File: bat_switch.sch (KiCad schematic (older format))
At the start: 7 parts

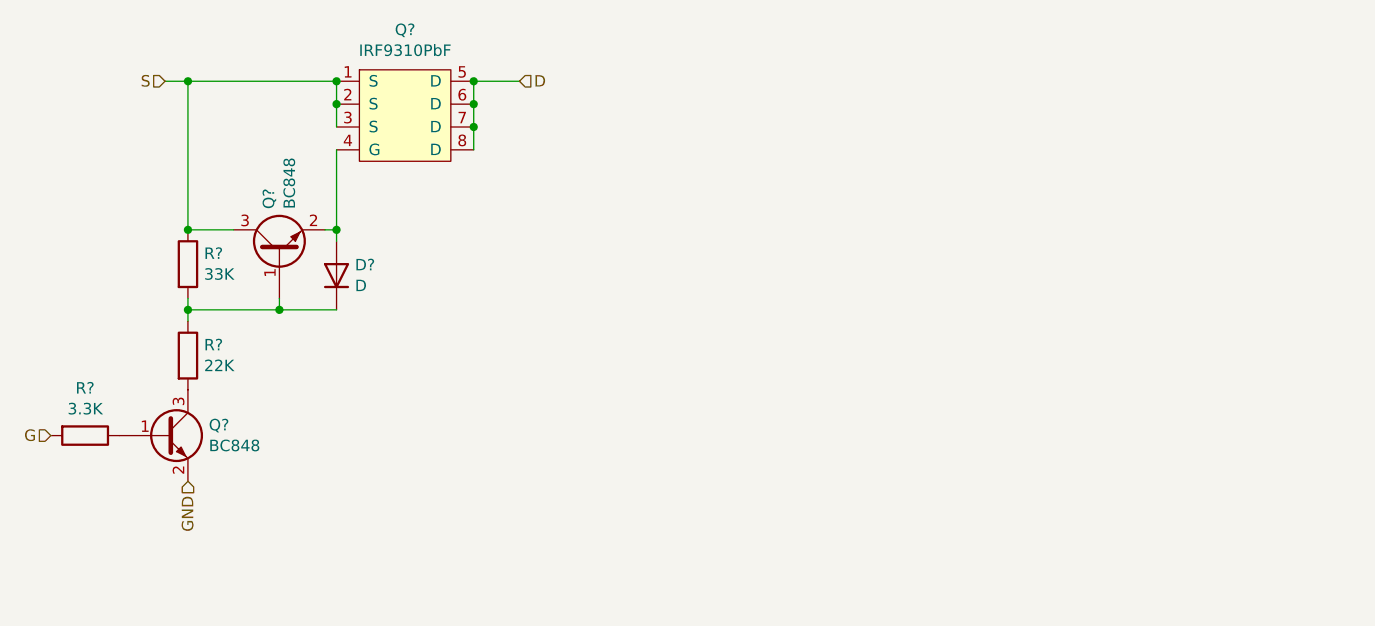
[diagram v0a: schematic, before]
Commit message: Fixes missing footprints, adds initial pcb
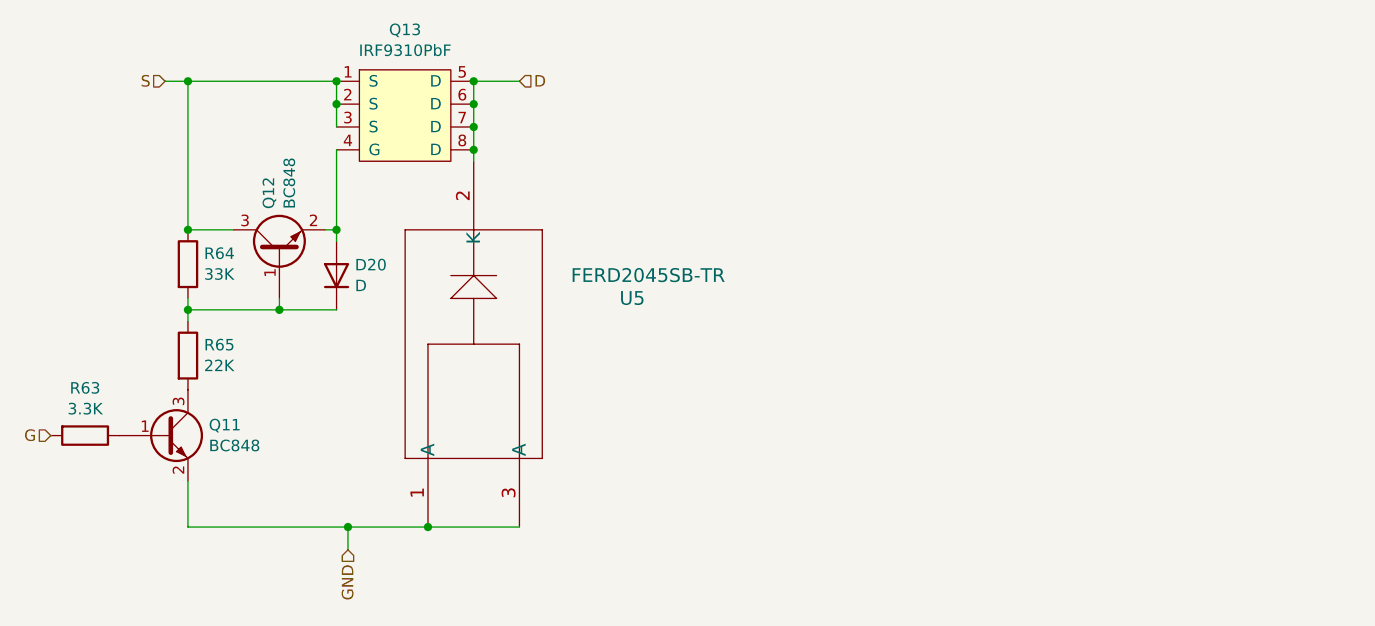
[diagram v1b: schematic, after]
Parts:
- added U5: FERD2045SB-TR, Package_TO_SOT_SMD:TO-263-2_TabPin1, symbol 2021-02-09_22-26-07:FERD2045SB-TR
- D20: renamed from D?; footprint (none) -> Diode_SMD:D_SMA
- gave numbers to parts that had none: 6
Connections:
- net D: now also U5.2 (K)
- net GND: now also U5.1 (A), U5.3 (A)
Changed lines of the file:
@@
 $Descr A4 11693 8268
 encoding utf-8
-Sheet 8 8
+Sheet 7 8
 Title ""
 Date ""
@@
 $EndDescr
 $Comp
-L Transistor_FET:IRF9310PbF Q?
+L Transistor_FET:IRF9310PbF Q13
 U 1 1 6023360E
 P 6050 2700
-F 0 "Q?" H 6050 3075 50  0000 C CNN
+F 0 "Q13" H 6050 3075 50  0000 C CNN
 F 1 "IRF9310PbF" H 6050 2984 50  0000 C CNN
 F 2 "Package_SO:SO-8_3.9x4.9mm_P1.27mm" H 6050 2700 50  0001 C CNN
@@
 $EndComp
 $Comp
-L Transistor_BJT:BC848 Q?
+L Transistor_BJT:BC848 Q11
 U 1 1 60234053
 P 5000 4100
-F 0 "Q?" H 5191 4146 50  0000 L CNN
+F 0 "Q11" H 5191 4146 50  0000 L CNN
 F 1 "BC848" H 5191 4055 50  0000 L CNN
 F 2 "Package_TO_SOT_SMD:SOT-23" H 5200 4025 50  0001 L CIN
@@
 $EndComp
 $Comp
-L Transistor_BJT:BC848 Q?
+L Transistor_BJT:BC848 Q12
 U 1 1 60234344
 P 5500 3300
-F 0 "Q?" H 5691 3346 50  0000 L CNN
+F 0 "Q12" H 5691 3346 50  0000 L CNN
 F 1 "BC848" H 5691 3255 50  0000 L CNN
 F 2 "Package_TO_SOT_SMD:SOT-23" H 5700 3225 50  0001 L CIN
@@
 $EndComp
 $Comp
-L Device:R R?
+L Device:R R63
 U 1 1 602349BB
 P 4650 4100
-F 0 "R?" V 4443 4100 50  0000 C CNN
+F 0 "R63" V 4443 4100 50  0000 C CNN
 F 1 "3.3K" V 4534 4100 50  0000 C CNN
 F 2 "Resistor_SMD:R_0805_2012Metric_Pad1.20x1.40mm_HandSolder" V 4580 4100 50  0001 C CNN
@@
 $EndComp
 $Comp
-L Device:R R?
+L Device:R R65
 U 1 1 60234C8A
 P 5100 3750
-F 0 "R?" H 5170 3796 50  0000 L CNN
+F 0 "R65" H 5170 3796 50  0000 L CNN
 F 1 "22K" H 5170 3705 50  0000 L CNN
 F 2 "Resistor_SMD:R_0805_2012Metric_Pad1.20x1.40mm_HandSolder" V 5030 3750 50  0001 C CNN
@@
 Text HLabel 4500 4100 0    50   Input ~ 0
 G
-Text HLabel 5100 4300 3    50   Input ~ 0
+Text HLabel 5800 4600 3    50   Input ~ 0
 GND
 $Comp
-L Device:R R?
+L Device:R R64
 U 1 1 6023A454
 P 5100 3350
-F 0 "R?" H 5170 3396 50  0000 L CNN
+F 0 "R64" H 5170 3396 50  0000 L CNN
 F 1 "33K" H 5170 3305 50  0000 L CNN
 F 2 "Resistor_SMD:R_0805_2012Metric_Pad1.20x1.40mm_HandSolder" V 5030 3350 50  0001 C CNN
@@
 	5100 3550 5100 3600
 $Comp
-L Device:D D?
+L Device:D D20
 U 1 1 6023F6A8
 P 5750 3400
-F 0 "D?" V 5796 3320 50  0000 R CNN
+F 0 "D20" V 5796 3320 50  0000 R CNN
 F 1 "D" V 5705 3320 50  0000 R CNN
-F 2 "" H 5750 3400 50  0001 C CNN
+F 2 "Diode_SMD:D_SMA" H 5750 3400 50  0001 C CNN
 F 3 "~" H 5750 3400 50  0001 C CNN
 	1    5750 3400
@@
 	6350 2550 6550 2550
 Connection ~ 6350 2550
+$Comp
+L 2021-02-09_22-26-07:FERD2045SB-TR U5
+U 1 1 6024EE1E
+P 6250 4500
+F 0 "U5" V 7250 3650 60  0000 L CNN
+F 1 "FERD2045SB-TR" V 7350 3300 60  0000 L CNN
+F 2 "Package_TO_SOT_SMD:TO-263-2_TabPin1" H 7050 4740 60  0001 C CNN
+F 3 "https://ar.mouser.com/datasheet/2/389/ferd2045s-1849465.pdf" V 7156 4728 60  0001 L CNN
+	1    6250 4500
+	0    -1   -1   0
+$EndComp
+Wire Wire Line
+	6350 2900 6350 2850
+Connection ~ 6350 2850
+Wire Wire Line
+	6550 4500 6150 4500
+Wire Wire Line
+	5100 4500 5100 4300
+Connection ~ 6150 4500
+Wire Wire Line
+	6150 4500 5800 4500
+Wire Wire Line
+	5800 4500 5800 4600
+Connection ~ 5800 4500
+Wire Wire Line
+	5800 4500 5100 4500
 $EndSCHEMATC

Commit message: Added mouser reference.com to charger imput molex pin
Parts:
- Q13: symbol Transistor_FET:IRF9310PbF -> bms_hardware-rescue:IRF9310PbF-Transistor_FET
- U5: symbol 2021-02-09_22-26-07:FERD2045SB-TR -> bms_hardware-rescue:FERD2045SB-TR-2021-02-09_22-26-07
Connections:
- net D: now also U5.3 (K); no longer U5.2 (K)
- net GND: now also U5.2 (A); no longer U5.3 (A)
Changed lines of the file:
@@
 $EndDescr
 $Comp
-L Transistor_FET:IRF9310PbF Q13
+L bms_hardware-rescue:IRF9310PbF-Transistor_FET Q13
 U 1 1 6023360E
 P 6050 2700
@@
 Connection ~ 6350 2550
 $Comp
-L 2021-02-09_22-26-07:FERD2045SB-TR U5
+L bms_hardware-rescue:FERD2045SB-TR-2021-02-09_22-26-07 U5
 U 1 1 6024EE1E
 P 6250 4500

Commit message: add minor changes to schs
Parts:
- U5: footprint Package_TO_SOT_SMD:TO-263-2_TabPin1 -> Package_TO_SOT_SMD:TO-263-3_TabPin2
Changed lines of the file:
@@
 F 0 "U5" V 7250 3650 60  0000 L CNN
 F 1 "FERD2045SB-TR" V 7350 3300 60  0000 L CNN
-F 2 "Package_TO_SOT_SMD:TO-263-2_TabPin1" H 7050 4740 60  0001 C CNN
+F 2 "Package_TO_SOT_SMD:TO-263-3_TabPin2" H 7050 4740 60  0001 C CNN
 F 3 "https://ar.mouser.com/datasheet/2/389/ferd2045s-1849465.pdf" V 7156 4728 60  0001 L CNN
 	1    6250 4500

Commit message: Adds final pcb
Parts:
- removed Q13: IRF9310PbF, Package_SO:SO-8_3.9x4.9mm_P1.27mm, symbol bms_hardware-rescue:IRF9310PbF-Transistor_FET
- removed U5: FERD2045SB-TR, Package_TO_SOT_SMD:TO-263-3_TabPin2, symbol bms_hardware-rescue:FERD2045SB-TR-2021-02-09_22-26-07
- added Q13: IRF9310PbF, Package_SO:SO-8_3.9x4.9mm_P1.27mm, symbol Transistor_FET:IRF9310PbF
- added U5: FERD2045SB-TR, Package_TO_SOT_SMD:TO-252-2, symbol 2021-02-09_22-26-07:FERD2045SB-TR
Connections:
- net D: now also Q13.5 (D), Q13.6 (D), Q13.7 (D), Q13.8 (D), U5.2 (K)
- net GND: now also U5.1 (A), U5.3 (A)
- net S: now also Q13.1 (S), Q13.2 (S), Q13.3 (S)
- net at D20.2 (A), Q12.2 (E): now also Q13.4 (G)
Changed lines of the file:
@@
 $Descr A4 11693 8268
 encoding utf-8
-Sheet 7 8
+Sheet 7 9
 Title ""
 Date ""
@@
 Comment4 ""
 $EndDescr
-$Comp
-L bms_hardware-rescue:IRF9310PbF-Transistor_FET Q13
-U 1 1 6023360E
-P 6050 2700
-F 0 "Q13" H 6050 3075 50  0000 C CNN
-F 1 "IRF9310PbF" H 6050 2984 50  0000 C CNN
-F 2 "Package_SO:SO-8_3.9x4.9mm_P1.27mm" H 6050 2700 50  0001 C CNN
-F 3 "https://ar.mouser.com/datasheet/2/196/irf9310pbf-1732564.pdf" H 6050 2700 50  0001 C CNN
-	1    6050 2700
-	1    0    0    -1
-$EndComp
 $Comp
 L Transistor_BJT:BC848 Q11
@@
 Connection ~ 5100 3200
 Wire Wire Line
-	5750 2550 5750 2650
-Connection ~ 5750 2550
-Connection ~ 5750 2650
-Wire Wire Line
-	5750 2650 5750 2750
-Wire Wire Line
 	5000 2550 5100 2550
 Connection ~ 5100 2550
@@
 D
 Wire Wire Line
-	6350 2550 6350 2650
-Connection ~ 6350 2650
-Wire Wire Line
-	6350 2650 6350 2750
-Connection ~ 6350 2750
-Wire Wire Line
-	6350 2750 6350 2850
-Wire Wire Line
 	6350 2550 6550 2550
-Connection ~ 6350 2550
-$Comp
-L bms_hardware-rescue:FERD2045SB-TR-2021-02-09_22-26-07 U5
-U 1 1 6024EE1E
-P 6250 4500
-F 0 "U5" V 7250 3650 60  0000 L CNN
-F 1 "FERD2045SB-TR" V 7350 3300 60  0000 L CNN
-F 2 "Package_TO_SOT_SMD:TO-263-3_TabPin2" H 7050 4740 60  0001 C CNN
-F 3 "https://ar.mouser.com/datasheet/2/389/ferd2045s-1849465.pdf" V 7156 4728 60  0001 L CNN
-	1    6250 4500
-	0    -1   -1   0
-$EndComp
-Wire Wire Line
-	6350 2900 6350 2850
-Connection ~ 6350 2850
-Wire Wire Line
-	6550 4500 6150 4500
 Wire Wire Line
 	5100 4500 5100 4300
-Connection ~ 6150 4500
-Wire Wire Line
-	6150 4500 5800 4500
 Wire Wire Line
 	5800 4500 5800 4600
@@
 Wire Wire Line
 	5800 4500 5100 4500
+Wire Wire Line
+	5800 4500 6150 4500
+$Comp
+L 2021-02-09_22-26-07:FERD2045SB-TR U5
+U 1 1 603F99FF
+P 6250 4500
+F 0 "U5" V 7156 4072 60  0000 R CNN
+F 1 "FERD2045SB-TR" V 7050 4072 60  0000 R CNN
+F 2 "Package_TO_SOT_SMD:TO-252-2" H 7050 4740 60  0001 C CNN
+F 3 "https://ar.mouser.com/datasheet/2/389/ferd2045s-1849465.pdf" V 6944 4072 60  0000 R CNN
+	1    6250 4500
+	0    -1   -1   0
+$EndComp
+$Comp
+L Transistor_FET:IRF9310PbF Q13
+U 1 1 603FB927
+P 6050 2700
+F 0 "Q13" H 6050 3075 50  0000 C CNN
+F 1 "IRF9310PbF" H 6050 2984 50  0000 C CNN
+F 2 "Package_SO:SO-8_3.9x4.9mm_P1.27mm" H 6050 2700 50  0001 C CNN
+F 3 "https://ar.mouser.com/datasheet/2/196/irf9310pbf-1732564.pdf" H 6050 2700 50  0001 C CNN
+	1    6050 2700
+	1    0    0    -1
+$EndComp
+Wire Wire Line
+	5750 2650 5750 2750
+Wire Wire Line
+	6350 2850 6350 2900
+Wire Wire Line
+	5750 2650 5750 2550
+Connection ~ 5750 2650
+Connection ~ 5750 2550
+Wire Wire Line
+	6350 2850 6350 2750
+Connection ~ 6350 2850
+Connection ~ 6350 2550
+Connection ~ 6350 2650
+Wire Wire Line
+	6350 2650 6350 2550
+Connection ~ 6350 2750
+Wire Wire Line
+	6350 2750 6350 2650
+Wire Wire Line
+	6150 4500 6550 4500
+Connection ~ 6150 4500
 $EndSCHEMATC
